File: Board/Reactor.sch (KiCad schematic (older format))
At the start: 10 parts, among them P1 CONN_02X13, P2 CONN_01X10, P3 CONN_01X13, P4 CONN_02X04, P5 USB_OTG, U1 74LS165

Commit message: -
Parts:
- removed P4: CONN_02X04, Pin_Headers:Pin_Header_Straight_2x04_Pitch2.54mm, symbol CONN_02X04
- added D1, D2, D3, D4: LED, LEDs:LED_D4.0mm, symbol LED
- P2: footprint Connectors_Molex:Molex_KK-6410-10_10x2.54mm_Straight -> Pin_Headers:Pin_Header_Angled_1x10_Pitch2.54mm
- P3: footprint Connectors_Molex:Molex_KK-6410-13_13x2.54mm_Straight -> Pin_Headers:Pin_Header_Straight_1x13_Pitch2.54mm
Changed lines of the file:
@@
 F 0 "P2" H 7400 3150 50  0000 C CNN
 F 1 "CONN_01X10" V 7500 2600 50  0000 C CNN
-F 2 "Connectors_Molex:Molex_KK-6410-10_10x2.54mm_Straight" H 7400 2600 50  0000 C CNN
+F 2 "Pin_Headers:Pin_Header_Angled_1x10_Pitch2.54mm" H 7400 2600 50  0000 C CNN
 F 3 "" H 7400 2600 50  0000 C CNN
 	1    7400 2600
@@
 F 0 "P3" H 2800 4750 50  0000 C CNN
 F 1 "CONN_01X13" V 2900 4050 50  0000 C CNN
-F 2 "Connectors_Molex:Molex_KK-6410-13_13x2.54mm_Straight" H 2800 4050 50  0000 C CNN
+F 2 "Pin_Headers:Pin_Header_Straight_1x13_Pitch2.54mm" H 2800 4050 50  0000 C CNN
 F 3 "" H 2800 4050 50  0000 C CNN
 	1    2800 4050
@@
 F 0 "R4" V 6180 5900 50  0000 C CNN
 F 1 "R" V 6100 5900 50  0000 C CNN
-F 2 "Resistors_ThroughHole:R_Axial_DIN0204_L3.6mm_D1.6mm_P7.62mm_Horizontal" V 6030 5900 50  0000 C CNN
+F 2 "Resistors_ThroughHole:R_Axial_DIN0204_L3.6mm_D1.6mm_P7.62mm_Horizontal" V 6030 5900 50  0001 C CNN
 F 3 "" H 6100 5900 50  0000 C CNN
 	1    6100 5900
@@
 F 0 "R3" V 6080 5900 50  0000 C CNN
 F 1 "R" V 6000 5900 50  0000 C CNN
-F 2 "Resistors_ThroughHole:R_Axial_DIN0204_L3.6mm_D1.6mm_P7.62mm_Horizontal" V 5930 5900 50  0000 C CNN
+F 2 "Resistors_ThroughHole:R_Axial_DIN0204_L3.6mm_D1.6mm_P7.62mm_Horizontal" V 5930 5900 50  0001 C CNN
 F 3 "" H 6000 5900 50  0000 C CNN
 	1    6000 5900
@@
 F 0 "R2" V 5980 5900 50  0000 C CNN
 F 1 "R" V 5900 5900 50  0000 C CNN
-F 2 "Resistors_ThroughHole:R_Axial_DIN0204_L3.6mm_D1.6mm_P7.62mm_Horizontal" V 5830 5900 50  0000 C CNN
+F 2 "Resistors_ThroughHole:R_Axial_DIN0204_L3.6mm_D1.6mm_P7.62mm_Horizontal" V 5830 5900 50  0001 C CNN
 F 3 "" H 5900 5900 50  0000 C CNN
 	1    5900 5900
@@
 F 0 "R1" V 5880 5900 50  0000 C CNN
 F 1 "R" V 5800 5900 50  0000 C CNN
-F 2 "Resistors_ThroughHole:R_Axial_DIN0204_L3.6mm_D1.6mm_P7.62mm_Horizontal" V 5730 5900 50  0000 C CNN
+F 2 "Resistors_ThroughHole:R_Axial_DIN0204_L3.6mm_D1.6mm_P7.62mm_Horizontal" V 5730 5900 50  0001 C CNN
 F 3 "" H 5800 5900 50  0000 C CNN
 	1    5800 5900
@@
 $EndComp
 Wire Wire Line
-	5800 6050 5800 6100
-Wire Wire Line
-	5900 6050 5900 6100
-Wire Wire Line
-	6000 6050 6000 6100
-Wire Wire Line
-	6100 6050 6100 6100
+	5800 6050 5800 6200
+Wire Wire Line
+	5900 6050 5900 6200
+Wire Wire Line
+	6000 6050 6000 6200
+Wire Wire Line
+	6100 6050 6100 6200
 Text Label 6150 4800 0    60   ~ 0
 LED1
@@
 Text Label 6250 5450 0    60   ~ 0
 LED3
-$Comp
-L CONN_02X04 P4
-U 1 1 587D6674
-P 5950 6350
-F 0 "P4" H 5950 6600 50  0000 C CNN
-F 1 "CONN_02X04" H 5950 6100 50  0000 C CNN
-F 2 "Pin_Headers:Pin_Header_Straight_2x04_Pitch2.54mm" H 5950 5150 50  0000 C CNN
-F 3 "" H 5950 5150 50  0000 C CNN
-	1    5950 6350
-	0    1    1    0
-$EndComp
-Wire Wire Line
-	5800 6600 5800 6700
-Wire Wire Line
-	5350 6700 6100 6700
+Wire Wire Line
+	5800 6500 5800 6700
+Wire Wire Line
+	6100 6700 5350 6700
 Wire Wire Line
 	5350 6700 5350 5100
 Connection ~ 5350 5100
 Wire Wire Line
-	5900 6700 5900 6600
+	5900 6500 5900 6700
 Connection ~ 5800 6700
 Wire Wire Line
-	6000 6700 6000 6600
+	6000 6500 6000 6700
 Connection ~ 5900 6700
 Wire Wire Line
-	6100 6700 6100 6600
+	6100 6500 6100 6700
 Connection ~ 6000 6700
 Text Label 6100 5650 0    60   ~ 0
@@
 Wire Wire Line
 	2950 2900 2950 2100
+$Comp
+L LED D4
+U 1 1 588687BE
+P 6100 6350
+F 0 "D4" H 6100 6450 50  0000 C CNN
+F 1 "LED" H 6100 6250 50  0000 C CNN
+F 2 "LEDs:LED_D4.0mm" H 6100 6350 50  0001 C CNN
+F 3 "" H 6100 6350 50  0000 C CNN
+	1    6100 6350
+	0    -1   -1   0
+$EndComp
+$Comp
+L LED D3
+U 1 1 588688D3
+P 6000 6350
+F 0 "D3" H 6000 6450 50  0000 C CNN
+F 1 "LED" H 6000 6250 50  0000 C CNN
+F 2 "LEDs:LED_D4.0mm" H 6000 6350 50  0001 C CNN
+F 3 "" H 6000 6350 50  0000 C CNN
+	1    6000 6350
+	0    -1   -1   0
+$EndComp
+$Comp
+L LED D2
+U 1 1 5886894F
+P 5900 6350
+F 0 "D2" H 5900 6450 50  0000 C CNN
+F 1 "LED" H 5900 6250 50  0000 C CNN
+F 2 "LEDs:LED_D4.0mm" H 5900 6350 50  0001 C CNN
+F 3 "" H 5900 6350 50  0000 C CNN
+	1    5900 6350
+	0    -1   -1   0
+$EndComp
+$Comp
+L LED D1
+U 1 1 58868983
+P 5800 6350
+F 0 "D1" H 5800 6450 50  0000 C CNN
+F 1 "LED" H 5800 6250 50  0000 C CNN
+F 2 "LEDs:LED_D4.0mm" H 5800 6350 50  0001 C CNN
+F 3 "" H 5800 6350 50  0000 C CNN
+	1    5800 6350
+	0    -1   -1   0
+$EndComp
 $EndSCHEMATC

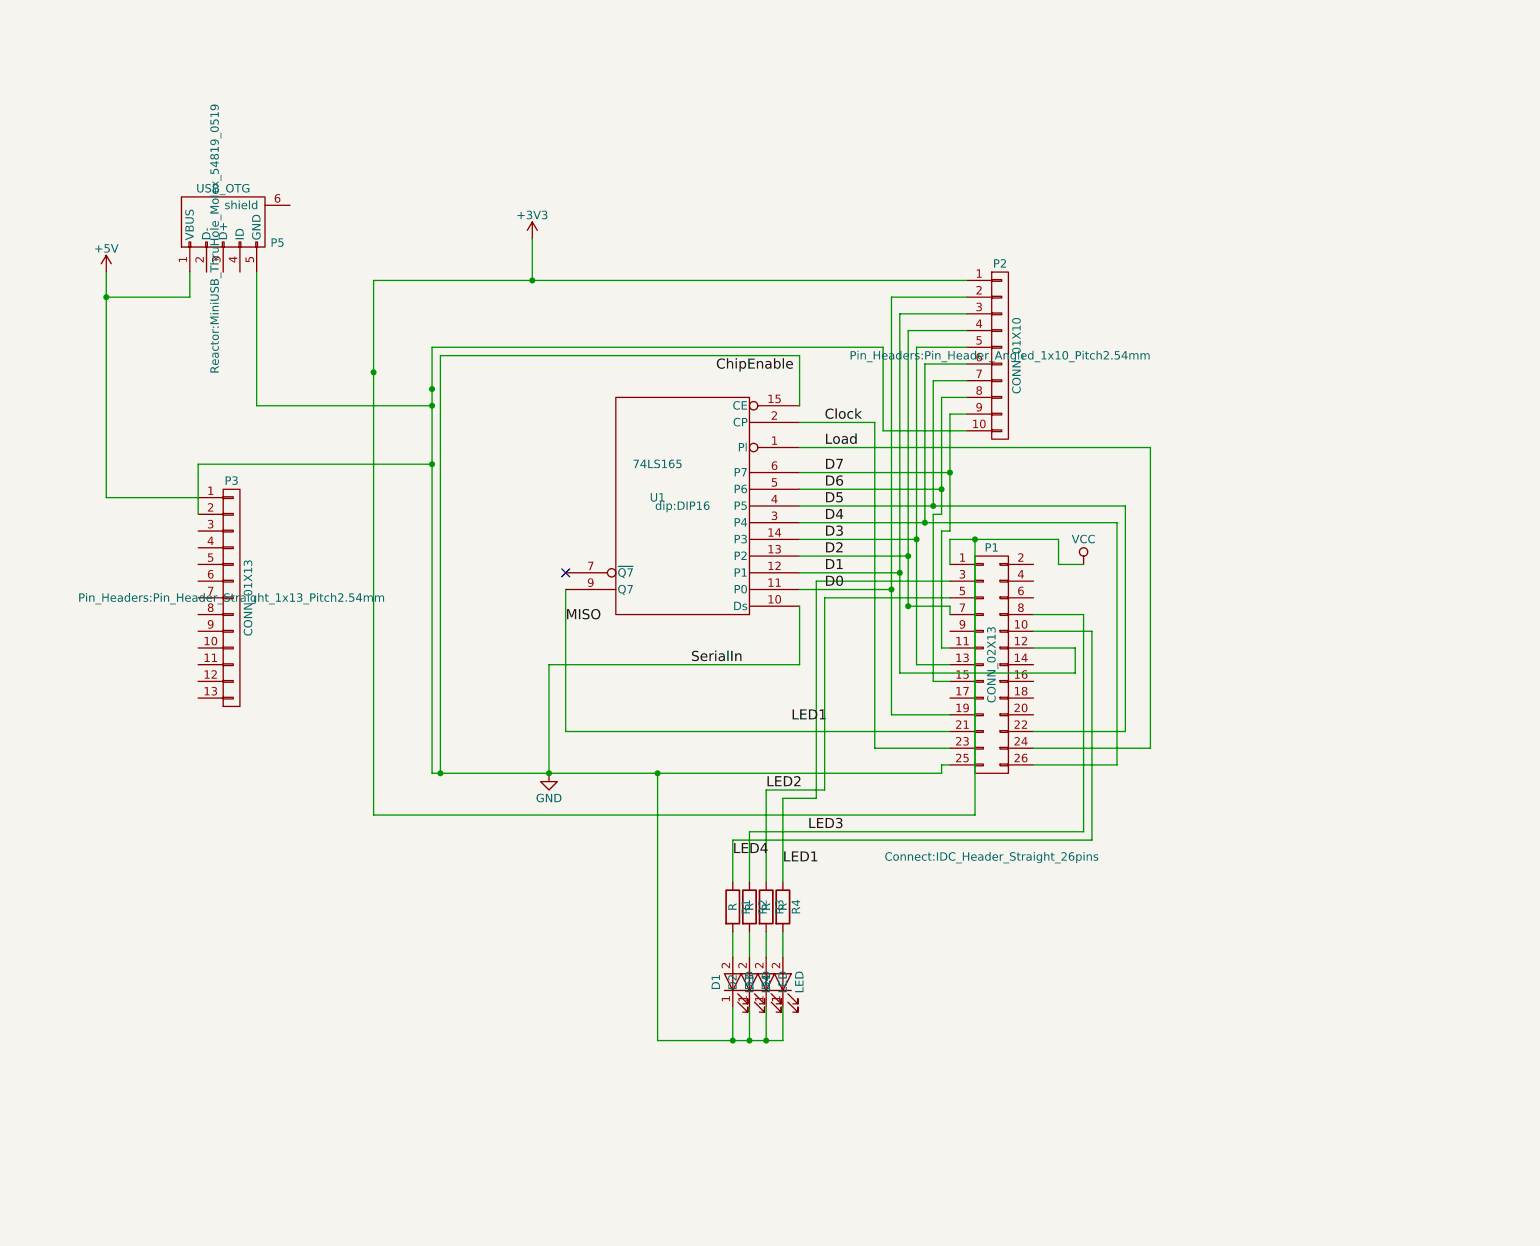
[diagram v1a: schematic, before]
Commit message: Started new design without shift register but with I2C I/O expander and direct I/O reads
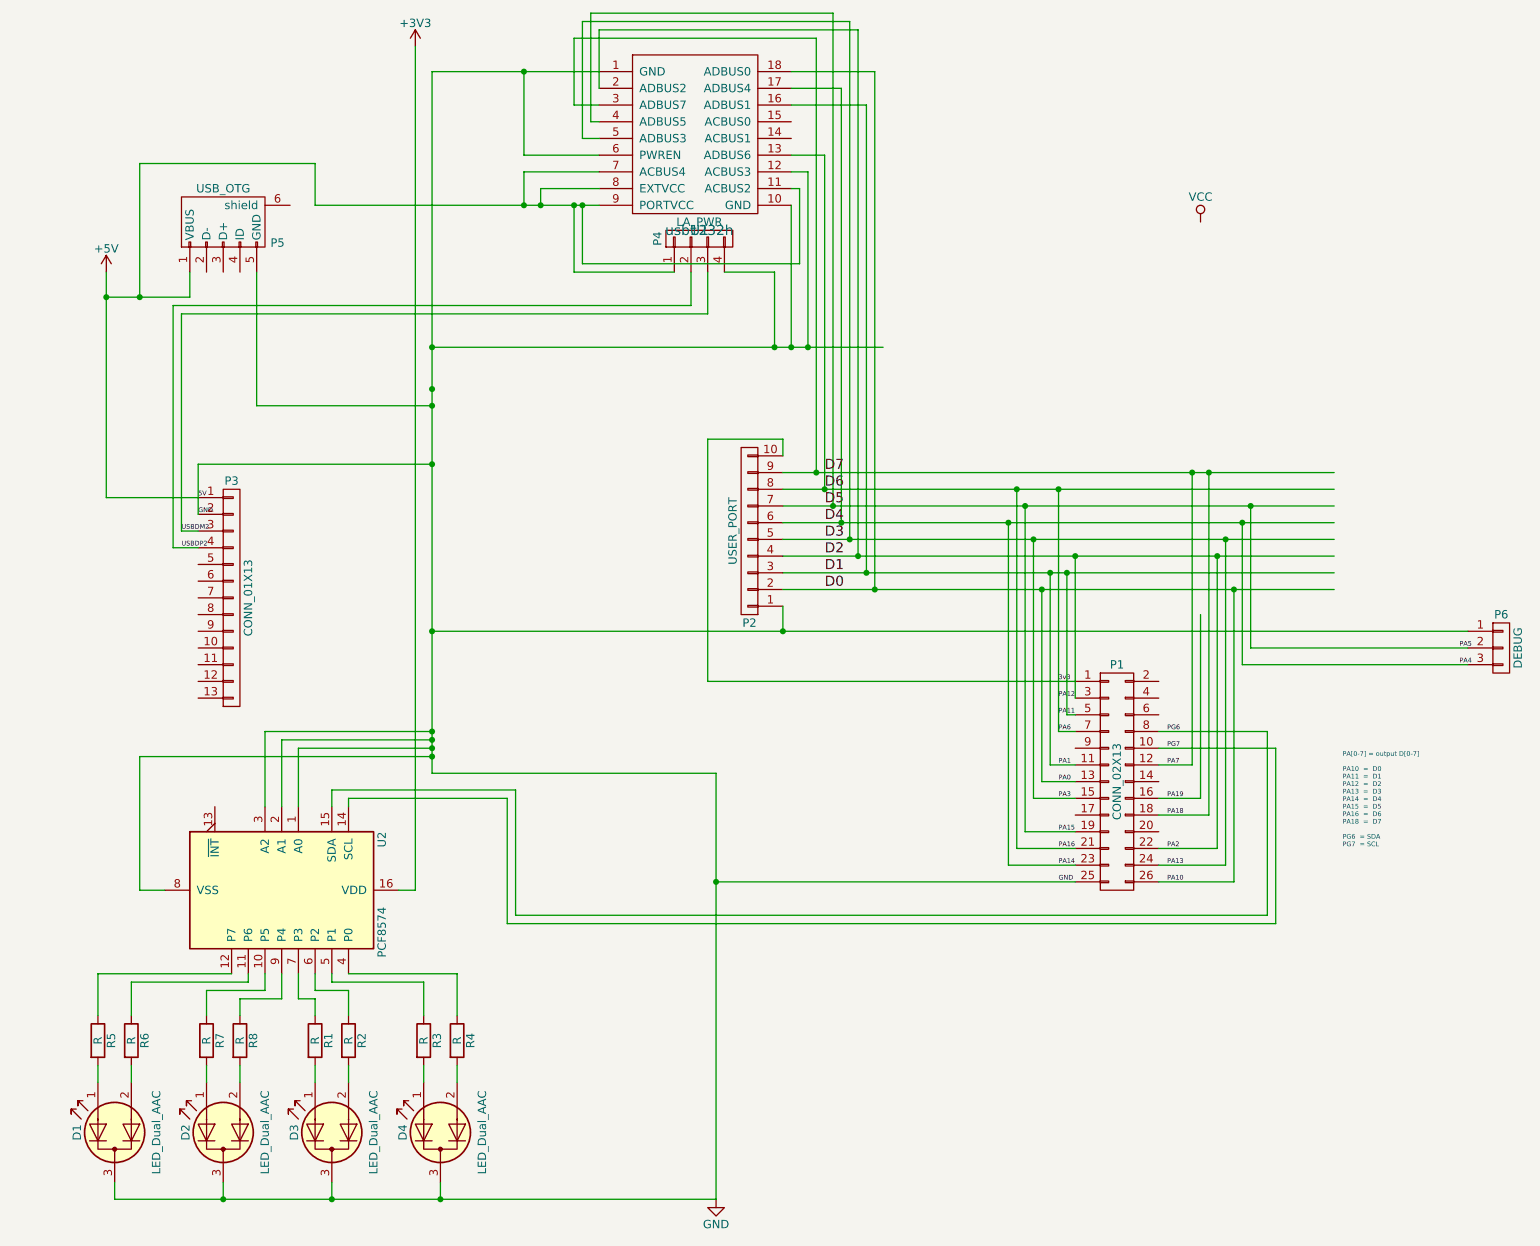
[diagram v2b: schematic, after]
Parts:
- removed D1, D2, D3, D4: LED, LEDs:LED_D4.0mm, symbol LED
- removed U1: 74LS165, dip:DIP16, symbol 74LS165
- added D1, D2, D3, D4: LED_Dual_AAC, LEDs_new:LED_D3.0mm-3, symbol LED_Dual_AAC
- added P4: LA_PWR, Connectors_Molex:Molex_KK-6410-04_04x2.54mm_Straight, symbol CONN_01X04
- added P6: DEBUG, Connectors_Molex:Molex_KK-6410-03_03x2.54mm_Straight, symbol CONN_01X03
- added R5, R6, R7, R8: R, Resistors_ThroughHole:R_Axial_DIN0204_L3.6mm_D1.6mm_P7.62mm_Horizontal, symbol R
- added U1: usb1232h, Housings_DIP:DIP-18_W7.62mm_LongPads, symbol usb1232h
- added U2: PCF8574, Housings_DIP:DIP-16_W7.62mm_LongPads, symbol PCF8574
- P2: value CONN_01X10 -> USER_PORT
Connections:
- net labels added: 3v3, 5V, PA0, PA1, PA10, PA11, PA12, PA13, PA14, PA15, PA16, PA18, PA19, PA2, PA3, PA4, PA5, PA6, PA7, PG6, PG7, USBDM2, USBDP2
- net labels removed: ChipEnable, Clock, LED1, LED2, LED3, LED4, Load, MISO, SerialIn
- wire segments 105 -> 171
- no-connect marks 1 -> 0
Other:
- note added: "PA[0-7] = output D[0-7]\n\nPA10 = D0\nPA11 = D1\nPA12 = D2\nPA13 = D3\nPA14 = D4\nPA15 = D5\nPA16 = D6\nPA18 = D7\n\nPG6 = SDA\nPG7 = SCL\n"
- moved on the sheet: P1, P2, R1, R2, R3, R4
